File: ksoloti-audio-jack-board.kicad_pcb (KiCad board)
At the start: 2 copper layers, 101 x 34 mm, 18 parts, among them J1 LINE_IN_OUT, J10 OUT_L_VOL, J11 OUT_R_VOL, J12 HP_VOL, J2 HP_OUT, J3 IN_L, J4 IN_R, J5 OUT_L, J6 OUT_R, J7 HP_OUT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

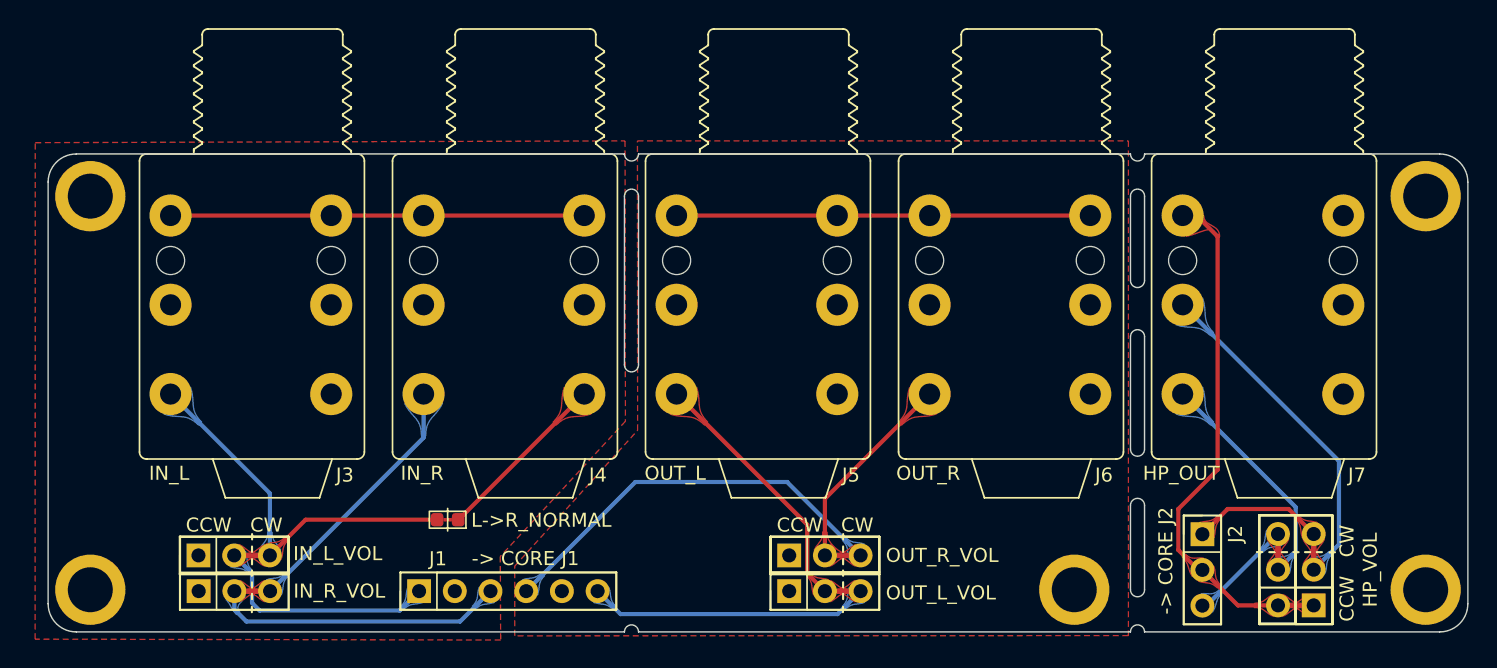
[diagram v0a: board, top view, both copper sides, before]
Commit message: update project (board dimensions now 100m*34mm)
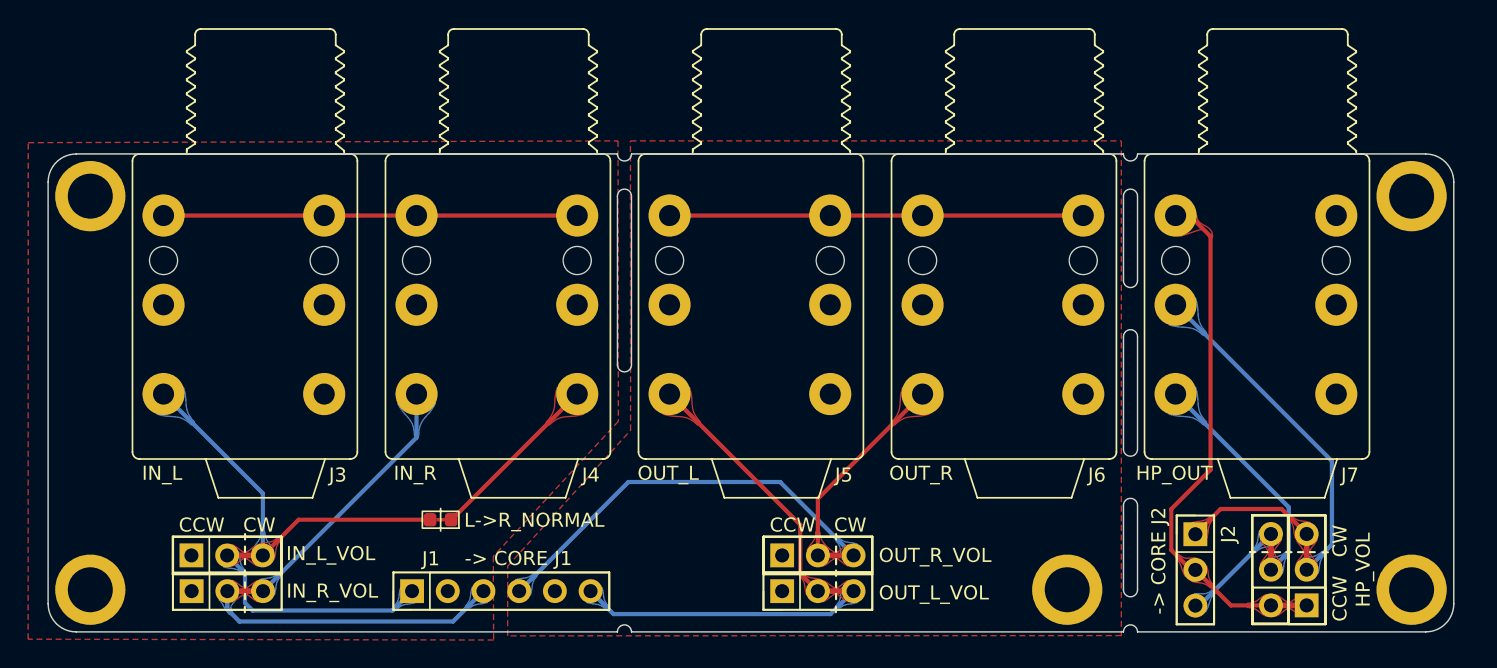
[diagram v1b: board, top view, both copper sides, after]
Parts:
- moved H3 1.00 mm to (168.3, 93.9)
- moved H5 1.00 mm to (168.3, 65.9)
- moved H4 0.50 mm to (143.8, 93.9)
- moved J1 0.50 mm to (97.2, 94.0)
- moved J10 0.50 mm to (123.5, 94.0)
- moved J11 0.50 mm to (123.5, 91.5)
- moved J12 0.50 mm to (160.8, 95.0)
- moved J2 0.50 mm to (152.9, 90.0)
- moved J3 0.50 mm to (79.5, 80.0)
- moved J4 0.50 mm to (97.5, 80.0)
- moved J5 0.50 mm to (115.5, 80.0)
- moved J6 0.50 mm to (133.5, 80.0)
- moved J7 0.50 mm to (151.5, 80.0)
- moved J8 0.50 mm to (81.5, 91.5)
- moved J9 0.50 mm to (81.5, 94.0)
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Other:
- board size 101 x 34 mm -> 100 x 34 mm
